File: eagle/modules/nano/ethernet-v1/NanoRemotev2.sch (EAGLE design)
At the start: 59 parts, among them IC1 ULN2803A, IC2 ULN2803A, IC4 ULN2803A

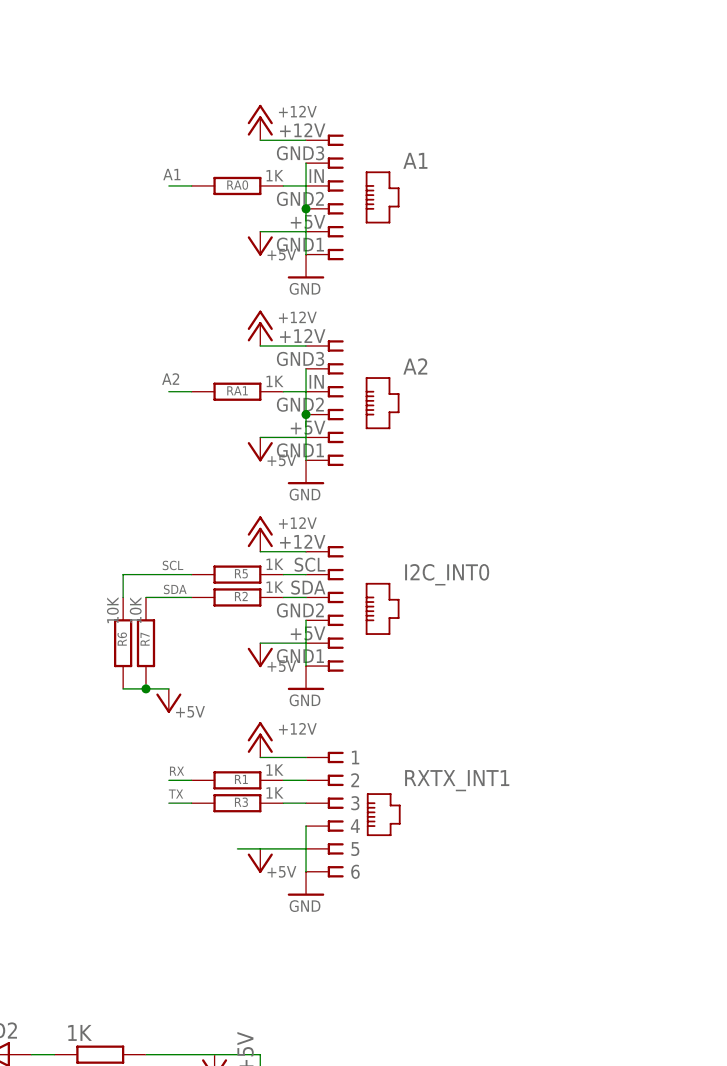
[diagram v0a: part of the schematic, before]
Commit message: Update extension and create new nano I2C
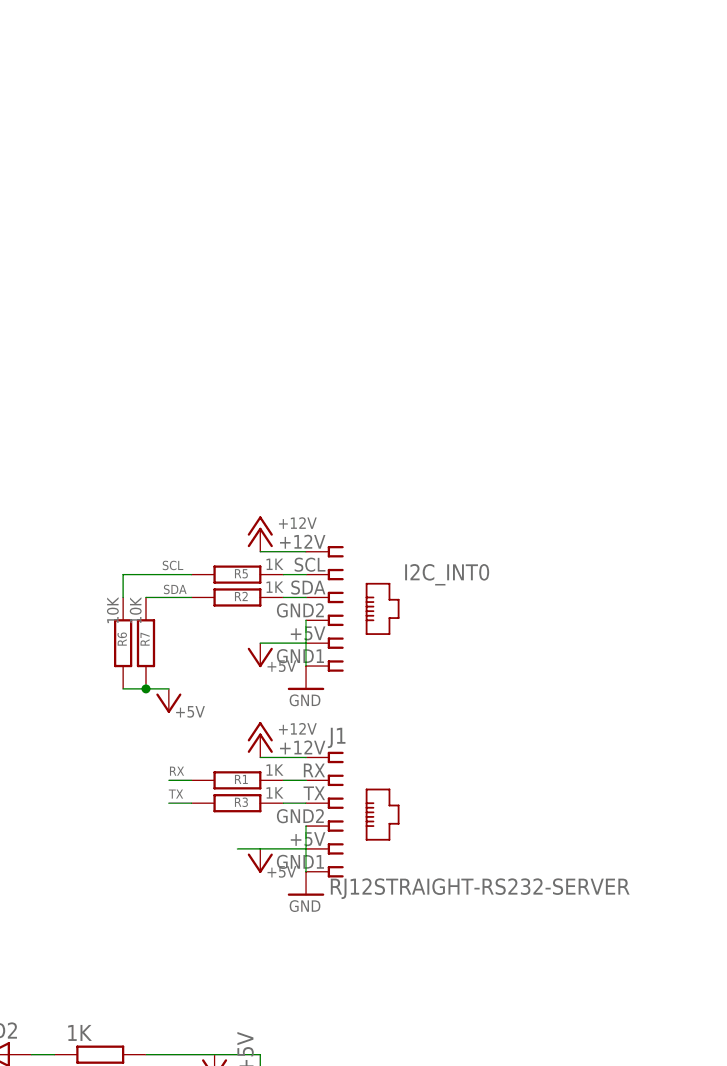
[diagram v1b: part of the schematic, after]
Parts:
- removed A1: ANALOG1, lpatiny:RJ12
- removed A2: ANALOG2, lpatiny:RJ12
- removed RA0, RA1: 1K, resistor:R-EU_M1206
- removed RXTX_INT1: RS232, lpatiny:RJ11-6XSTRAIGHT
- added J1: RJ12STRAIGHT-RS232-SERVER, lpatiny:RJ12STRAIGHT-RS232-SERVER
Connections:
- removed net D2B8: A1.3, RA0.1
- removed net D2B9: A2.3, RA1.1
- net +12V: now also J1.1; no longer A1.1, A2.1, RXTX_INT1.1
- net +5V: now also J1.5; no longer A1.5, A2.5, RXTX_INT1.5
- net A1: no longer RA0.2
- net A2: no longer RA1.2
- net D2B5: now also J1.3; no longer RXTX_INT1.3
- net GND: now also J1.4, J1.6; no longer A1.2, A1.4, A1.6, A2.2, A2.4, A2.6, RXTX_INT1.4, RXTX_INT1.6
- net N$7: now also J1.2; no longer RXTX_INT1.2
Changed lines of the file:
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@@
 <part name="IC1" library="lpatiny" deviceset="ULN2803A" device="" value="ULN2803A"/>
 <part name="GND6" library="supply1" deviceset="GND" device=""/>
-<part name="RXTX_INT1" library="lpatiny" deviceset="RJ11" device="STRAIGHT" technology="-6X" value="RS232"/>
 <part name="GND11" library="supply1" deviceset="GND" device=""/>
 <part name="P+14" library="supply1" deviceset="+5V" device=""/>
@@
 <part name="LED1" library="lpatiny" deviceset="LED3MM" device="" value=""/>
 <part name="FRAME1" library="frames" deviceset="DINA3_L" device=""/>
-<part name="A1" library="lpatiny" deviceset="RJ12" device="" value="ANALOG1"/>
-<part name="GND17" library="supply1" deviceset="GND" device=""/>
-<part name="P+24" library="supply1" deviceset="+5V" device=""/>
-<part name="P+25" library="supply1" deviceset="+12V" device=""/>
-<part name="RA0" library="resistor" deviceset="R-EU_" device="M1206" value="1K"/>
-<part name="A2" library="lpatiny" deviceset="RJ12" device="" value="ANALOG2"/>
-<part name="GND18" library="supply1" deviceset="GND" device=""/>
-<part name="P+26" library="supply1" deviceset="+5V" device=""/>
-<part name="P+29" library="supply1" deviceset="+12V" device=""/>
-<part name="RA1" library="resistor" deviceset="R-EU_" device="M1206" value="1K"/>
 <part name="RGB_5-6-11" library="lpatiny" deviceset="TOPLED-3" device=""/>
 <part name="RGB_7-8-13" library="lpatiny" deviceset="TOPLED-3" device=""/>
@@
 <part name="R6" library="resistor" deviceset="R-EU_" device="M1206" value="10K"/>
 <part name="R7" library="resistor" deviceset="R-EU_" device="M1206" value="10K"/>
+<part name="J1" library="lpatiny" deviceset="RJ12" device="STRAIGHT-RS232-SERVER"/>
 </parts>
 <sheets>
@@
 <attribute name="VALUE" x="41.275" y="165.735" size="1.27" layer="96"/>
 </instance>
-<instance part="RXTX_INT1" gate="G$1" x="335.28" y="152.4" smashed="yes">
-<attribute name="NAME" x="343.535" y="154.305" size="1.778" layer="95"/>
-</instance>
 <instance part="GND11" gate="1" x="332.74" y="142.24" smashed="yes">
 <attribute name="VALUE" x="330.835" y="140.335" size="1.27" layer="96"/>
@@
 <instance part="FRAME1" gate="G$1" x="0" y="0"/>
 <instance part="FRAME1" gate="G$2" x="287.02" y="0"/>
-<instance part="A1" gate="G$1" x="335.28" y="220.98" smashed="yes">
-<attribute name="NAME" x="343.535" y="222.885" size="1.778" layer="95"/>
-</instance>
-<instance part="GND17" gate="1" x="332.74" y="210.82" smashed="yes">
-<attribute name="VALUE" x="330.835" y="208.915" size="1.27" layer="96"/>
-</instance>
-<instance part="P+24" gate="1" x="327.66" y="213.36" smashed="yes" rot="R180">
-<attribute name="VALUE" x="328.295" y="212.725" size="1.27" layer="96"/>
-</instance>
-<instance part="P+25" gate="1" x="327.66" y="228.6" smashed="yes">
-<attribute name="VALUE" x="329.565" y="228.6" size="1.27" layer="96"/>
-</instance>
-<instance part="RA0" gate="G$1" x="325.12" y="220.98" smashed="yes" rot="MR0">
-<attribute name="NAME" x="326.39" y="220.5736" size="1.016" layer="95" rot="MR0"/>
-<attribute name="VALUE" x="330.2" y="221.488" size="1.27" layer="96" rot="MR0"/>
-</instance>
-<instance part="A2" gate="G$1" x="335.28" y="198.12" smashed="yes">
-<attribute name="NAME" x="343.535" y="200.025" size="1.778" layer="95"/>
-</instance>
-<instance part="GND18" gate="1" x="332.74" y="187.96" smashed="yes">
-<attribute name="VALUE" x="330.835" y="186.055" size="1.27" layer="96"/>
-</instance>
-<instance part="P+26" gate="1" x="327.66" y="190.5" smashed="yes" rot="R180">
-<attribute name="VALUE" x="328.295" y="189.865" size="1.27" layer="96"/>
-</instance>
-<instance part="P+29" gate="1" x="327.66" y="205.74" smashed="yes">
-<attribute name="VALUE" x="329.565" y="205.74" size="1.27" layer="96"/>
-</instance>
-<instance part="RA1" gate="G$1" x="325.12" y="198.12" smashed="yes" rot="MR0">
-<attribute name="NAME" x="326.39" y="197.7136" size="1.016" layer="95" rot="MR0"/>
-<attribute name="VALUE" x="330.2" y="198.628" size="1.27" layer="96" rot="MR0"/>
-</instance>
 <instance part="RGB_5-6-11" gate="G$1" x="142.24" y="220.98" rot="R270"/>
 <instance part="RGB_7-8-13" gate="G$1" x="142.24" y="200.66" rot="R270"/>
@@
 <attribute name="VALUE" x="314.452" y="175.26" size="1.27" layer="96" rot="MR270"/>
 </instance>
+<instance part="J1" gate="G$1" x="335.28" y="152.4"/>
 </instances>
 <busses>
@@
 </segment>
 <segment>
-<wire x1="332.74" y1="144.78" x2="332.74" y2="149.86" width="0.1524" layer="91"/>
-<pinref part="RXTX_INT1" gate="G$1" pin="6"/>
-<pinref part="RXTX_INT1" gate="G$1" pin="4"/>
-<pinref part="GND11" gate="1" pin="GND"/>
-</segment>
-<segment>
 <wire x1="104.14" y1="157.48" x2="104.14" y2="162.56" width="0.1524" layer="91"/>
 <pinref part="D2_IO5" gate="G$1" pin="6"/>
@@
 <pinref part="D3_IO6" gate="G$1" pin="4"/>
 <pinref part="GND16" gate="1" pin="GND"/>
-</segment>
-<segment>
-<wire x1="332.74" y1="213.36" x2="332.74" y2="218.44" width="0.1524" layer="91"/>
-<wire x1="332.74" y1="223.52" x2="332.74" y2="218.44" width="0.1524" layer="91"/>
-<junction x="332.74" y="218.44"/>
-<pinref part="A1" gate="G$1" pin="6"/>
-<pinref part="A1" gate="G$1" pin="4"/>
-<pinref part="GND17" gate="1" pin="GND"/>
-<pinref part="A1" gate="G$1" pin="2"/>
-</segment>
-<segment>
-<wire x1="332.74" y1="190.5" x2="332.74" y2="195.58" width="0.1524" layer="91"/>
-<wire x1="332.74" y1="200.66" x2="332.74" y2="195.58" width="0.1524" layer="91"/>
-<junction x="332.74" y="195.58"/>
-<pinref part="A2" gate="G$1" pin="6"/>
-<pinref part="A2" gate="G$1" pin="4"/>
-<pinref part="GND18" gate="1" pin="GND"/>
-<pinref part="A2" gate="G$1" pin="2"/>
 </segment>
 <segment>
@@
 <pinref part="RA3" gate="G$1" pin="2"/>
 </segment>
+<segment>
+<pinref part="GND11" gate="1" pin="GND"/>
+<pinref part="J1" gate="G$1" pin="6"/>
+<pinref part="J1" gate="G$1" pin="4"/>
+<wire x1="332.74" y1="149.86" x2="332.74" y2="144.78" width="0.1524" layer="91"/>
+</segment>
 </net>
 <net name="+12V" class="2">
@@
 <segment>
 <wire x1="332.74" y1="157.48" x2="327.66" y2="157.48" width="0.1524" layer="91"/>
-<pinref part="RXTX_INT1" gate="G$1" pin="1"/>
 <pinref part="P+19" gate="1" pin="+12V"/>
+<pinref part="J1" gate="G$1" pin="1"/>
 </segment>
 <segment>
@@
 <pinref part="D3_IO6" gate="G$1" pin="1"/>
 <pinref part="P+23" gate="1" pin="+12V"/>
-</segment>
-<segment>
-<wire x1="332.74" y1="226.06" x2="327.66" y2="226.06" width="0.1524" layer="91"/>
-<pinref part="A1" gate="G$1" pin="1"/>
-<pinref part="P+25" gate="1" pin="+12V"/>
-</segment>
-<segment>
-<wire x1="332.74" y1="203.2" x2="327.66" y2="203.2" width="0.1524" layer="91"/>
-<pinref part="A2" gate="G$1" pin="1"/>
-<pinref part="P+29" gate="1" pin="+12V"/>
 </segment>
 <segment>
@@
 <wire x1="327.66" y1="147.32" x2="332.74" y2="147.32" width="0.1524" layer="91"/>
 <wire x1="325.12" y1="147.32" x2="327.66" y2="147.32" width="0.1524" layer="91"/>
-<pinref part="RXTX_INT1" gate="G$1" pin="5"/>
 <pinref part="P+14" gate="1" pin="+5V"/>
+<pinref part="J1" gate="G$1" pin="5"/>
 </segment>
 <segment>
@@
 <pinref part="P+22" gate="1" pin="+5V"/>
 <pinref part="RL1" gate="G$1" pin="2"/>
-</segment>
-<segment>
-<wire x1="327.66" y1="215.9" x2="332.74" y2="215.9" width="0.1524" layer="91"/>
-<pinref part="A1" gate="G$1" pin="5"/>
-<pinref part="P+24" gate="1" pin="+5V"/>
-</segment>
-<segment>
-<wire x1="327.66" y1="193.04" x2="332.74" y2="193.04" width="0.1524" layer="91"/>
-<pinref part="A2" gate="G$1" pin="5"/>
-<pinref part="P+26" gate="1" pin="+5V"/>
 </segment>
 <segment>
@@
 <pinref part="ARDUINO1" gate="ARDUINO" pin="A1"/>
 </segment>
-<segment>
-<wire x1="320.04" y1="220.98" x2="317.5" y2="220.98" width="0.1524" layer="91"/>
-<label x="316.865" y="221.615" size="1.27" layer="95"/>
-<pinref part="RA0" gate="G$1" pin="2"/>
-</segment>
 </net>
 <net name="A2" class="0">
@@
 <label x="228.6" y="227.965" size="1.27" layer="95"/>
 <pinref part="ARDUINO1" gate="ARDUINO" pin="A2"/>
-</segment>
-<segment>
-<wire x1="320.04" y1="198.12" x2="317.5" y2="198.12" width="0.1524" layer="91"/>
-<label x="316.738" y="198.882" size="1.27" layer="95"/>
-<pinref part="RA1" gate="G$1" pin="2"/>
 </segment>
 </net>
@@
 <segment>
 <wire x1="332.74" y1="152.4" x2="330.2" y2="152.4" width="0.1524" layer="91"/>
-<pinref part="RXTX_INT1" gate="G$1" pin="3"/>
 <pinref part="R3" gate="G$1" pin="1"/>
+<pinref part="J1" gate="G$1" pin="3"/>
 </segment>
 </net>
@@
 <pinref part="D3_IO6" gate="G$1" pin="3"/>
 <pinref part="R1B" gate="G$1" pin="1"/>
-</segment>
-</net>
-<net name="D2B8" class="0">
-<segment>
-<wire x1="332.74" y1="220.98" x2="330.2" y2="220.98" width="0.1524" layer="91"/>
-<pinref part="A1" gate="G$1" pin="3"/>
-<pinref part="RA0" gate="G$1" pin="1"/>
-</segment>
-</net>
-<net name="D2B9" class="0">
-<segment>
-<wire x1="332.74" y1="198.12" x2="330.2" y2="198.12" width="0.1524" layer="91"/>
-<pinref part="A2" gate="G$1" pin="3"/>
-<pinref part="RA1" gate="G$1" pin="1"/>
 </segment>
 </net>
@@
 <wire x1="330.2" y1="154.94" x2="332.74" y2="154.94" width="0.1524" layer="91"/>
 <pinref part="R1" gate="G$1" pin="1"/>
-<pinref part="RXTX_INT1" gate="G$1" pin="2"/>
-</segment>
-</net>
+<pinref part="J1" gate="G$1" pin="2"/>
+</segment>
+</net>
